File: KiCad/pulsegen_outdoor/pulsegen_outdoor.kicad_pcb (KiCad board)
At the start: 4 copper layers, 65 x 40 mm, 31 parts, among them J1 Conn_Coaxial, J2 Conn_Coaxial, U1 ADCMP572, U2 LT1963AxST-3.3

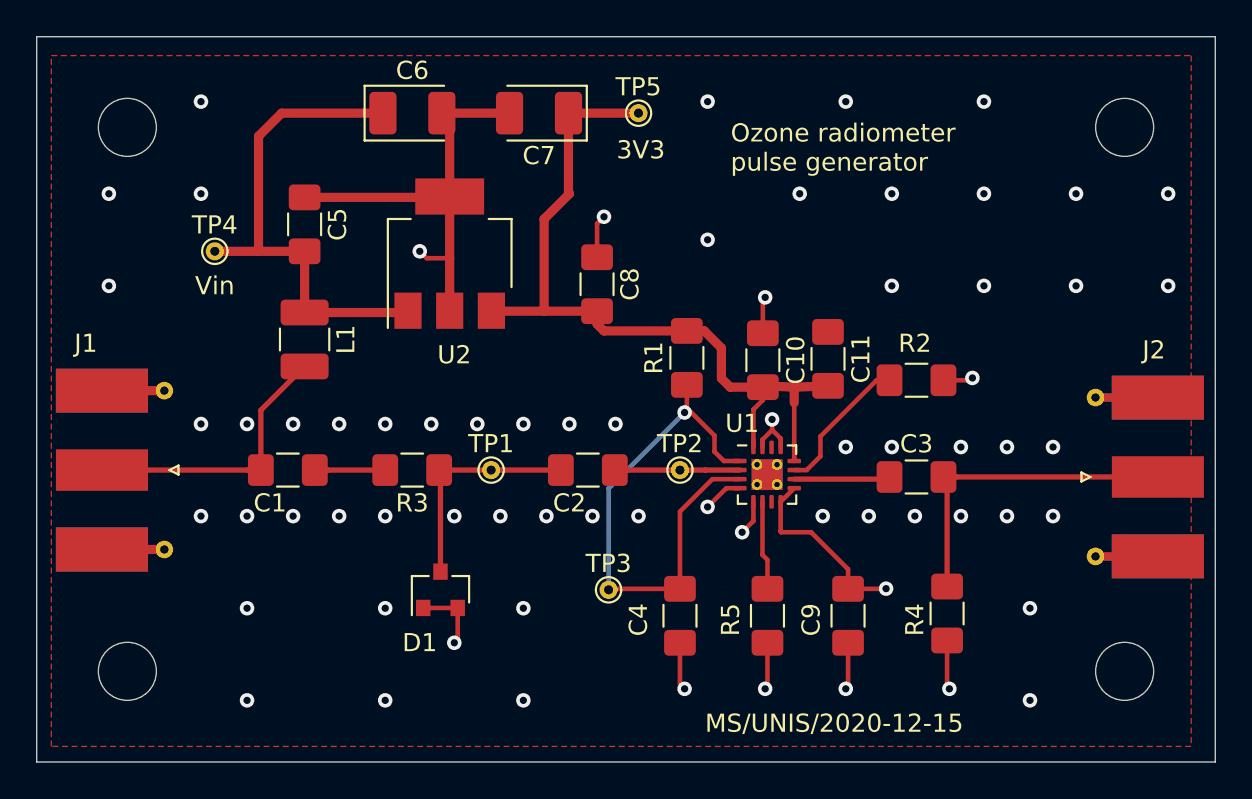
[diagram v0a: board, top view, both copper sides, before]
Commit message: Add indoor unit
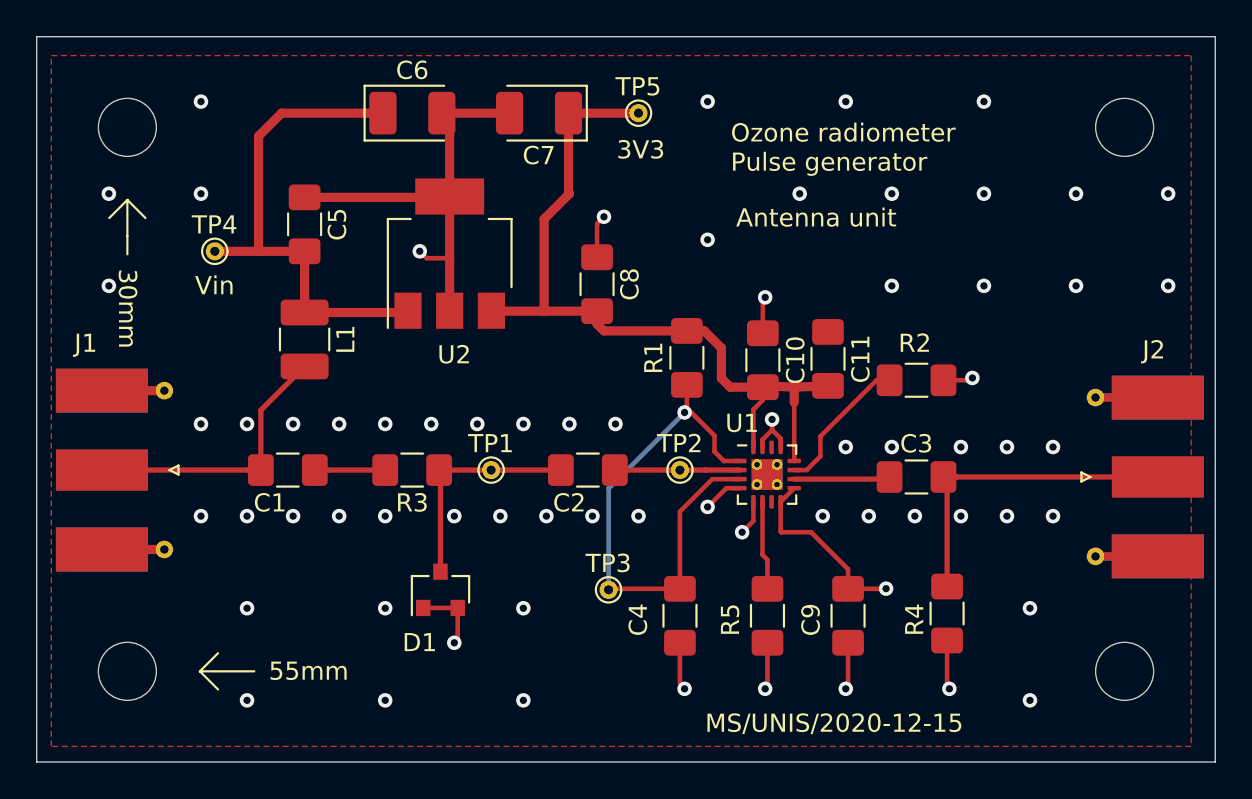
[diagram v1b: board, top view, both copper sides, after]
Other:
- board text added: "30mm"
- board text added: "55mm"
- board text added: "Antenna unit"
- board text added: "Ozone radiometer Pulse generator"
- board text removed: "Ozone radiometer pulse generator"
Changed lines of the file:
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@@
   (general
     (thickness 1.6)
-    (drawings 8)
+    (drawings 20)
     (tracks 200)
     (zones 0)
@@
   )
   (setup
-    (last_trace_width 0.508)
+    (last_trace_width 0.254)
     (user_trace_width 0.29337)
     (user_trace_width 0.508)
@@
     (visible_elements 7FFDFFFF)
     (pcbplotparams
-      (layerselection 0x010fc_ffffffff)
+      (layerselection 0x00000_7ffffff9)
       (usegerberextensions false)
       (usegerberattributes false)
       (usegerberadvancedattributes false)
       (creategerberjobfile false)
-      (excludeedgelayer true)
+      (excludeedgelayer false)
       (linewidth 0.100000)
       (plotframeref false)
@@
       (padsonsilk false)
       (subtractmaskfromsilk false)
-      (outputformat 1)
+      (outputformat 4)
       (mirror false)
-      (drillshape 1)
+      (drillshape 0)
       (scaleselection 1)
       (outputdirectory ""))
@@
     (pad 1 np_thru_hole circle (at 0 0) (size 3.2 3.2) (drill 3.2) (layers *.Cu *.Mask))
   )
+  (gr_text "Antenna unit" (at 133 75) (layer F.SilkS)
+    (effects (font (size 1 1) (thickness 0.15)))
+  )
+  (gr_text 30mm (at 95 80 270) (layer F.SilkS)
+    (effects (font (size 1 1) (thickness 0.15)))
+  )
+  (gr_line (start 95 77) (end 95 76) (layer F.SilkS) (width 0.12))
+  (gr_line (start 95 74) (end 94 75) (layer F.SilkS) (width 0.12))
+  (gr_line (start 95 74) (end 96 75) (layer F.SilkS) (width 0.12))
+  (gr_line (start 95 76) (end 95 74) (layer F.SilkS) (width 0.12))
+  (gr_text 55mm (at 105 100) (layer F.SilkS)
+    (effects (font (size 1 1) (thickness 0.15)))
+  )
+  (gr_line (start 99 100) (end 100 101) (layer F.SilkS) (width 0.12))
+  (gr_line (start 99 100) (end 100 99) (layer F.SilkS) (width 0.12))
+  (gr_line (start 102 100) (end 99 100) (layer F.SilkS) (width 0.12))
+  (dimension 55 (width 0.15) (layer Dwgs.User)
+    (gr_text "55.000 mm" (at 122.5 111.299999) (layer Dwgs.User)
+      (effects (font (size 1 1) (thickness 0.15)))
+    )
+    (feature1 (pts (xy 150 100) (xy 150 110.58642)))
+    (feature2 (pts (xy 95 100) (xy 95 110.58642)))
+    (crossbar (pts (xy 95 109.999999) (xy 150 109.999999)))
+    (arrow1a (pts (xy 150 109.999999) (xy 148.873496 110.58642)))
+    (arrow1b (pts (xy 150 109.999999) (xy 148.873496 109.413578)))
+    (arrow2a (pts (xy 95 109.999999) (xy 96.126504 110.58642)))
+    (arrow2b (pts (xy 95 109.999999) (xy 96.126504 109.413578)))
+  )
+  (dimension 30 (width 0.15) (layer Dwgs.User)
+    (gr_text "30.000 mm" (at 68.7 85 270) (layer Dwgs.User)
+      (effects (font (size 1 1) (thickness 0.15)))
+    )
+    (feature1 (pts (xy 95 100) (xy 69.413579 100)))
+    (feature2 (pts (xy 95 70) (xy 69.413579 70)))
+    (crossbar (pts (xy 70 70) (xy 70 100)))
+    (arrow1a (pts (xy 70 100) (xy 69.413579 98.873496)))
+    (arrow1b (pts (xy 70 100) (xy 70.586421 98.873496)))
+    (arrow2a (pts (xy 70 70) (xy 69.413579 71.126504)))
+    (arrow2b (pts (xy 70 70) (xy 70.586421 71.126504)))
+  )
   (gr_text MS/UNIS/2020-12-15 (at 133.985 102.87) (layer F.SilkS)
     (effects (font (size 1 1) (thickness 0.15)))
   )
-  (gr_text "Ozone radiometer\npulse generator" (at 128.27 71.12) (layer F.SilkS)
+  (gr_text "Ozone radiometer\nPulse generator" (at 128.27 71.12) (layer F.SilkS)
     (effects (font (size 1 1) (thickness 0.15)) (justify left))
   )
